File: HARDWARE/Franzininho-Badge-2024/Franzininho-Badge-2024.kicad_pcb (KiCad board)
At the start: 2 copper layers, 96 x 64 mm, 68 parts, among them J1 UART, J2 SWIO, J3 SPI, Q1 SIL2308, SW1 USER, SW2 ON, SW3 RESET, U1 CH32V003F4P6, U2 OLED 128x64 1.3", U3 1.54in 200x200, U4 2.13in 250x122

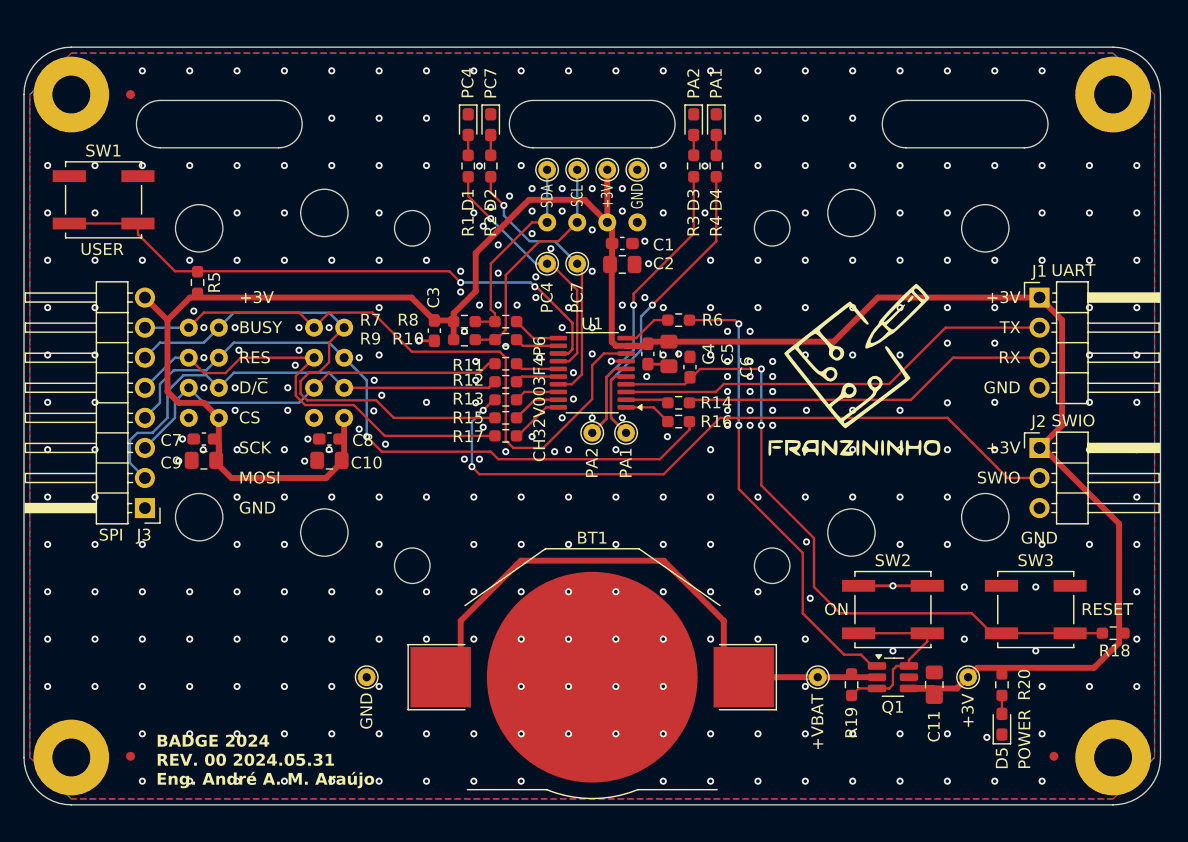
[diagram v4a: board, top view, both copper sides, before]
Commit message: Finalização do esquemático e layout.
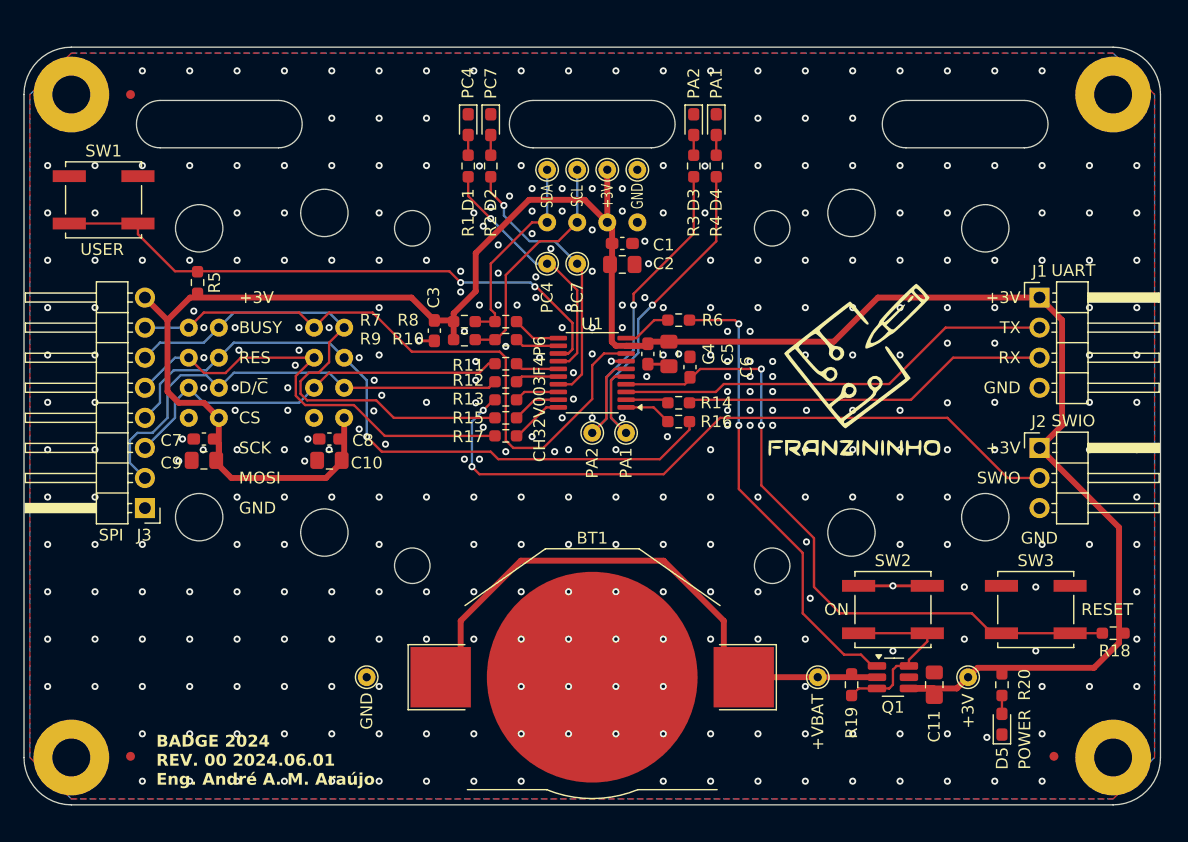
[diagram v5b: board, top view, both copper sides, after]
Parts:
- U3: value 1.54in 200x200 -> EPD 200x200 1.54"
- U4: value 2.13in 250x122 -> EPD 250x122 2.13"
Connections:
- net Net-(D1-A) renamed /LED PC7
- net Net-(D2-A) renamed /LED PC4
- net Net-(D3-A) renamed /LED PA2
- net Net-(D4-A) renamed /LED PA1
- net Net-(D5-A) renamed /LED POWER
- net Net-(Q1A-D1) renamed /SWITCH ~{ON}
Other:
- board text added: "BADGE 2024 REV. 00 2024.06.01 Eng. André A. M. Araújo"
- board text removed: "BADGE 2024 REV. 00 2024.05.31 Eng. André A. M. Araújo"
